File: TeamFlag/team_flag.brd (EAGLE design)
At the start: 40.6 x 40.6 mm, 24 parts, among them Q1 IRFML8244, Q2 IRFML8244

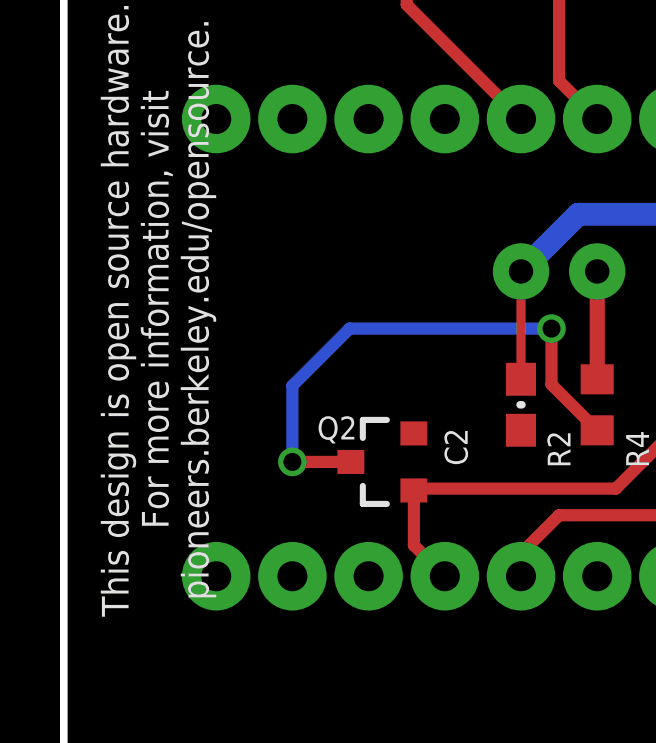
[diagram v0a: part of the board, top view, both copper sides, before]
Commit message: REVIEW CHECK: Fix name on APM
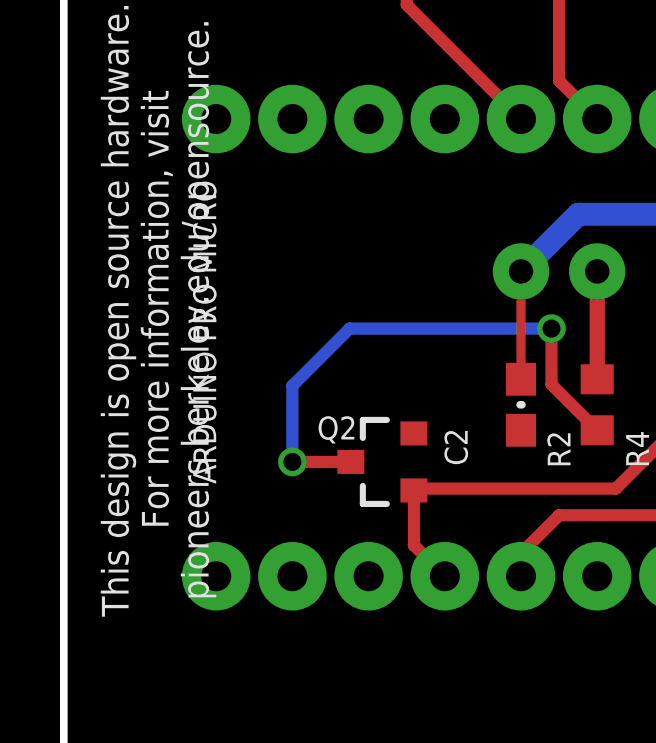
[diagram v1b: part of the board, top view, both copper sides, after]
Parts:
- renumbered U$3 to APM
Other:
- board text added: "ARDUINO PRO MICRO"
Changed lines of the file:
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@@
 <setting verticaltext="up"/>
 </settings>
-<grid distance="0.05" unitdist="inch" unit="inch" style="lines" multiple="1" display="yes" altdistance="0.005" altunitdist="inch" altunit="inch"/>
+<grid distance="0.01" unitdist="inch" unit="inch" style="lines" multiple="1" display="yes" altdistance="0.005" altunitdist="inch" altunit="inch"/>
 <layers>
 <layer number="1" name="Top" color="4" fill="1" visible="yes" active="yes"/>
@@
 For more information, visit
 pioneers.berkeley.edu/opensource.</text>
+<text x="4.318" y="23.368" size="0.762" layer="25" font="vector" rot="R270">ARDUINO PRO MICRO</text>
 </plain>
 <attributes>
@@
 <attribute name="VALUE" x="5.45880625" y="31.758984375" size="0.762" layer="26" font="vector" ratio="15" rot="MR309" align="center"/>
 </element>
-<element name="U$3" library="pie" package="ARDUINO_PRO_MICRO" value="ARDUINO_PRO_MICRO" x="3.81" y="8.89" smashed="yes" rot="MR90"/>
+<element name="APM" library="pie" package="ARDUINO_PRO_MICRO" value="ARDUINO_PRO_MICRO" x="3.81" y="8.89" smashed="yes" rot="MR90"/>
 </elements>
 <signals>
@@
 <contactref element="Q2" pad="1"/>
 <contactref element="R4" pad="2"/>
-<contactref element="U$3" pad="6"/>
+<contactref element="APM" pad="6"/>
 <wire x1="12.7" y1="10.16" x2="11.668" y2="11.192" width="0.4064" layer="1"/>
 <wire x1="11.668" y1="11.192" x2="11.668" y2="13.02" width="0.4064" layer="1"/>
@@
 <vertex x="40.64" y="40.64"/>
 </polygon>
-<contactref element="U$3" pad="GND@1"/>
-<contactref element="U$3" pad="GND@0"/>
-<contactref element="U$3" pad="GND@2"/>
+<contactref element="APM" pad="GND@1"/>
+<contactref element="APM" pad="GND@0"/>
+<contactref element="APM" pad="GND@2"/>
 </signal>
 <signal name="BLUE(IO1)">
 <contactref element="Q1" pad="1"/>
 <contactref element="R3" pad="2"/>
-<contactref element="U$3" pad="5"/>
+<contactref element="APM" pad="5"/>
 <wire x1="15.24" y1="10.16" x2="15.24" y2="10.922" width="0.4064" layer="1"/>
 <wire x1="15.24" y1="10.922" x2="16.51" y2="12.192" width="0.4064" layer="1"/>
@@
 <wire x1="23.495" y1="22.225" x2="17.145" y2="22.225" width="0.762" layer="16"/>
 <wire x1="17.145" y1="22.225" x2="15.24" y2="20.32" width="0.762" layer="16"/>
-<contactref element="U$3" pad="VCC"/>
+<contactref element="APM" pad="VCC"/>
 <wire x1="25.4" y1="20.32" x2="25.4" y2="25.4" width="0.762" layer="1"/>
 </signal>
 <signal name="LED4">
 <contactref element="R8" pad="2"/>
-<contactref element="U$3" pad="A0"/>
+<contactref element="APM" pad="A0"/>
 <wire x1="15.24" y1="25.4" x2="11.43" y2="29.21" width="0.4064" layer="1"/>
 <wire x1="11.43" y1="29.21" x2="11.43" y2="30.9" width="0.4064" layer="1"/>
@@
 <contactref element="R5" pad="2"/>
 <wire x1="26.67" y1="30.9" x2="24.55" y2="30.9" width="0.3048" layer="1"/>
-<contactref element="U$3" pad="A3"/>
+<contactref element="APM" pad="A3"/>
 <wire x1="22.86" y1="25.4" x2="26.67" y2="29.21" width="0.4064" layer="1"/>
 <wire x1="26.67" y1="29.21" x2="26.67" y2="30.9" width="0.4064" layer="1"/>
@@
 <signal name="LED2">
 <contactref element="R6" pad="2"/>
-<contactref element="U$3" pad="A2"/>
+<contactref element="APM" pad="A2"/>
 <wire x1="20.32" y1="25.4" x2="21.59" y2="26.67" width="0.4064" layer="1"/>
 <wire x1="21.59" y1="26.67" x2="21.59" y2="30.9" width="0.4064" layer="1"/>
@@
 <signal name="LED3">
 <contactref element="R7" pad="2"/>
-<contactref element="U$3" pad="A1"/>
+<contactref element="APM" pad="A1"/>
 <wire x1="17.78" y1="25.4" x2="16.51" y2="26.67" width="0.4064" layer="1"/>
 <wire x1="16.51" y1="26.67" x2="16.51" y2="30.9" width="0.4064" layer="1"/>

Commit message: Minor fixes everywhere
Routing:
- net LED2: track 6.03 -> 5.31 mm
- net LED1: track 9.20 -> 8.48 mm
- net 5V: track 20.4 -> 20.9 mm
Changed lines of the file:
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@@
 <contactref element="R4" pad="2"/>
 <contactref element="APM" pad="6"/>
-<wire x1="12.7" y1="10.16" x2="11.668" y2="11.192" width="0.4064" layer="1"/>
+<wire x1="13.208" y1="10.668" x2="11.668" y2="11.192" width="0.4064" layer="1"/>
 <wire x1="11.668" y1="11.192" x2="11.668" y2="13.02" width="0.4064" layer="1"/>
 <wire x1="11.668" y1="13.02" x2="11.729" y2="13.081" width="0.4064" layer="1"/>
@@
 <contactref element="R3" pad="2"/>
 <contactref element="APM" pad="5"/>
-<wire x1="15.24" y1="10.16" x2="15.24" y2="10.922" width="0.4064" layer="1"/>
+<wire x1="15.748" y1="10.668" x2="15.24" y2="10.922" width="0.4064" layer="1"/>
 <wire x1="15.24" y1="10.922" x2="16.51" y2="12.192" width="0.4064" layer="1"/>
 <wire x1="16.51" y1="12.192" x2="24.765" y2="12.192" width="0.4064" layer="1"/>
@@
 <wire x1="17.145" y1="22.225" x2="15.24" y2="20.32" width="0.762" layer="16"/>
 <contactref element="APM" pad="VCC"/>
-<wire x1="25.4" y1="20.32" x2="25.4" y2="25.4" width="0.762" layer="1"/>
+<wire x1="25.4" y1="20.32" x2="25.908" y2="25.908" width="0.762" layer="1"/>
 </signal>
 <signal name="LED4">
 <contactref element="R8" pad="2"/>
 <contactref element="APM" pad="A0"/>
-<wire x1="15.24" y1="25.4" x2="11.43" y2="29.21" width="0.4064" layer="1"/>
+<wire x1="15.748" y1="25.908" x2="11.43" y2="29.21" width="0.4064" layer="1"/>
 <wire x1="11.43" y1="29.21" x2="11.43" y2="30.9" width="0.4064" layer="1"/>
 </signal>
@@
 <wire x1="26.67" y1="30.9" x2="24.55" y2="30.9" width="0.3048" layer="1"/>
 <contactref element="APM" pad="A3"/>
-<wire x1="22.86" y1="25.4" x2="26.67" y2="29.21" width="0.4064" layer="1"/>
+<wire x1="23.368" y1="25.908" x2="26.67" y2="29.21" width="0.4064" layer="1"/>
 <wire x1="26.67" y1="29.21" x2="26.67" y2="30.9" width="0.4064" layer="1"/>
 </signal>
@@
 <contactref element="R6" pad="2"/>
 <contactref element="APM" pad="A2"/>
-<wire x1="20.32" y1="25.4" x2="21.59" y2="26.67" width="0.4064" layer="1"/>
+<wire x1="20.828" y1="25.908" x2="21.59" y2="26.67" width="0.4064" layer="1"/>
 <wire x1="21.59" y1="26.67" x2="21.59" y2="30.9" width="0.4064" layer="1"/>
 </signal>
@@
 <contactref element="R7" pad="2"/>
 <contactref element="APM" pad="A1"/>
-<wire x1="17.78" y1="25.4" x2="16.51" y2="26.67" width="0.4064" layer="1"/>
+<wire x1="18.288" y1="25.908" x2="16.51" y2="26.67" width="0.4064" layer="1"/>
 <wire x1="16.51" y1="26.67" x2="16.51" y2="30.9" width="0.4064" layer="1"/>
 </signal>

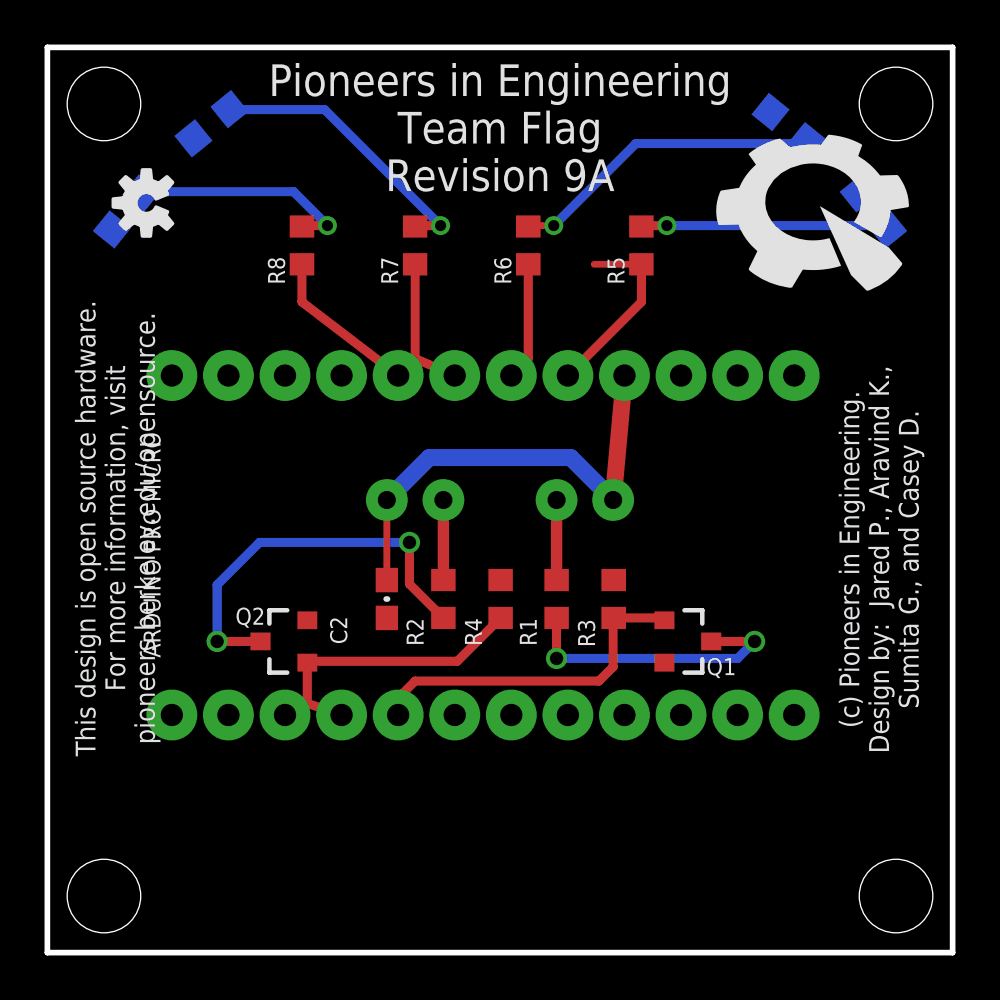
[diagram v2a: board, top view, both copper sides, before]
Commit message: APM mirrored and rerouted
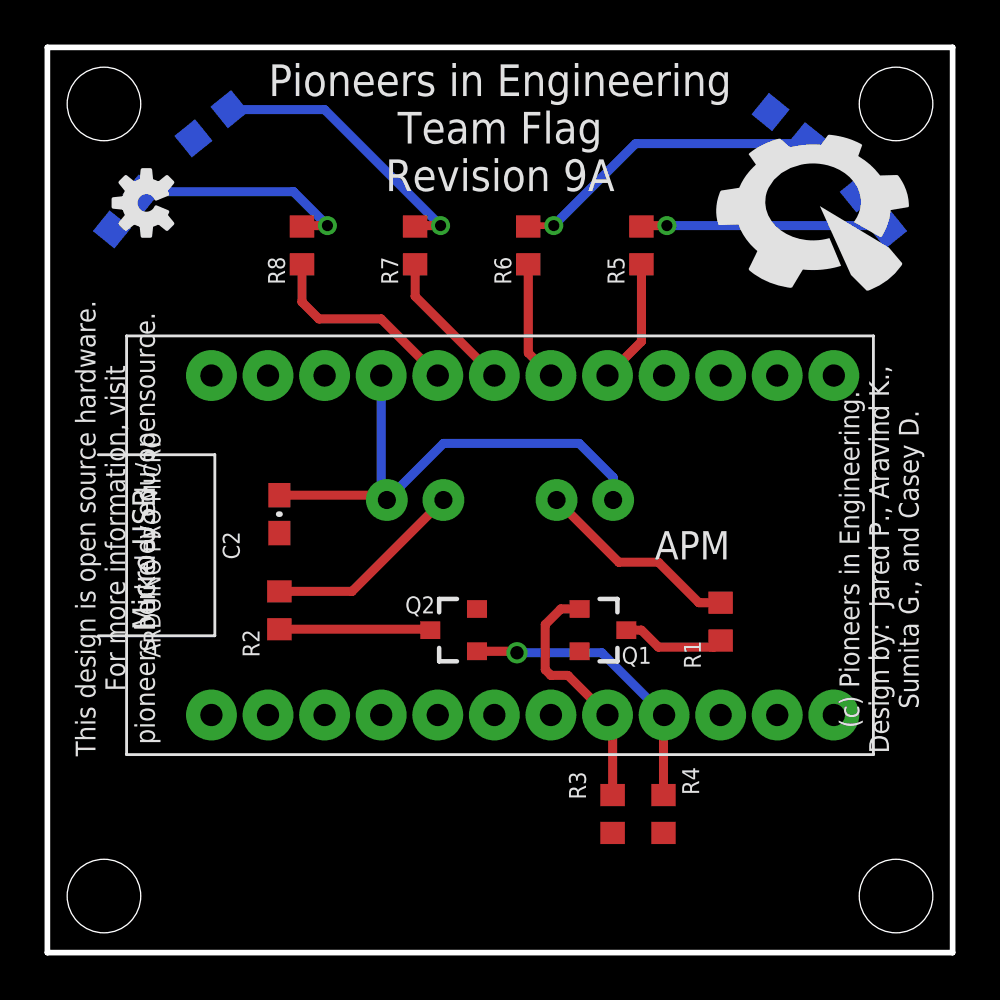
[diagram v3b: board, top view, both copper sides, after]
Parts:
- moved APM 33.3 mm to (37.1, 8.89), flipped to the top
- moved R4 12.1 mm to (27.7, 6.22), turned to 90 degrees
- moved R3 9.65 mm to (25.4, 6.22), turned to 90 degrees
- moved Q2 7.64 mm to (18.3, 14.5)
- moved R1 7.44 mm to (30.2, 14.9)
- moved R2 7.38 mm to (10.4, 15.4)
- moved C2 6.15 mm to (10.4, 19.7)
- moved Q1 3.84 mm to (24.9, 14.5)
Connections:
- net LED1: now also APM.A0; no longer APM.A3
- net LED2: now also APM.A1; no longer APM.A2
- net LED3: now also APM.A2; no longer APM.A1
- net LED4: now also APM.A3; no longer APM.A0
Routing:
- net YSOURCE: track 17.9 -> 6.79 mm, vias 2 -> 0
- net BSOURCE: track 13.0 -> 4.67 mm, vias 2 -> 0
- net N$2: track 3.59 -> 9.28 mm
- net N$3: track 3.59 -> 9.07 mm
- net BLUE(IO1): track 16.0 -> 11.2 mm
- net LED1: track 8.48 -> 5.62 mm
- net 5V: track 20.9 -> 23.5 mm
- net LED4: track 7.13 -> 9.15 mm
- net YELLOW(IO2): track 13.0 -> 13.2 mm, vias 0 -> 1
